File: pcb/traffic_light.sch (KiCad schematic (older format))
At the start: 48 parts, among them J1 Serial, J2 Power, Q1 BS170, Q2 BS170, Q3 BS170, SW1 RESET, SW2 FLASH, U1 ESP-12F, U2 LM1117-3.3

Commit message: start assigning footprints
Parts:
- U1: footprint (none) -> ESP8266:ESP-12E_SMD
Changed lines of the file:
@@
 F 0 "U1" H 6330 3085 50  0000 C CNN
 F 1 "ESP-12F" H 6330 2994 50  0000 C CNN
-F 2 "" H 6330 2320 50  0001 C CNN
+F 2 "ESP8266:ESP-12E_SMD" H 6330 2320 50  0001 C CNN
 F 3 "" H 6330 2320 50  0001 C CNN
 	1    6330 2320

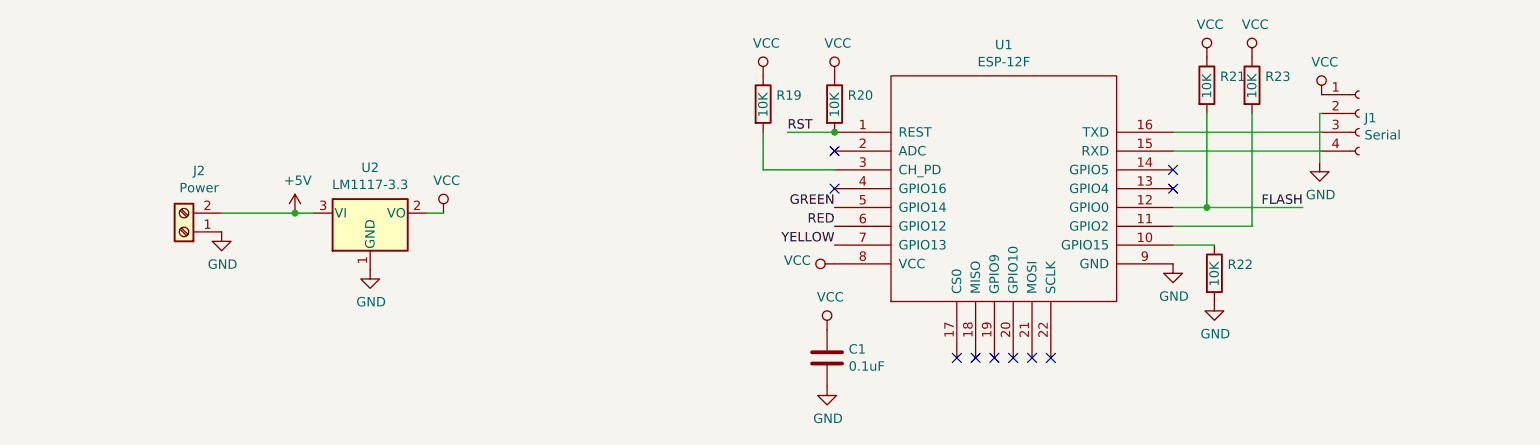
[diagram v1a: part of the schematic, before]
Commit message: start laying out the PCB
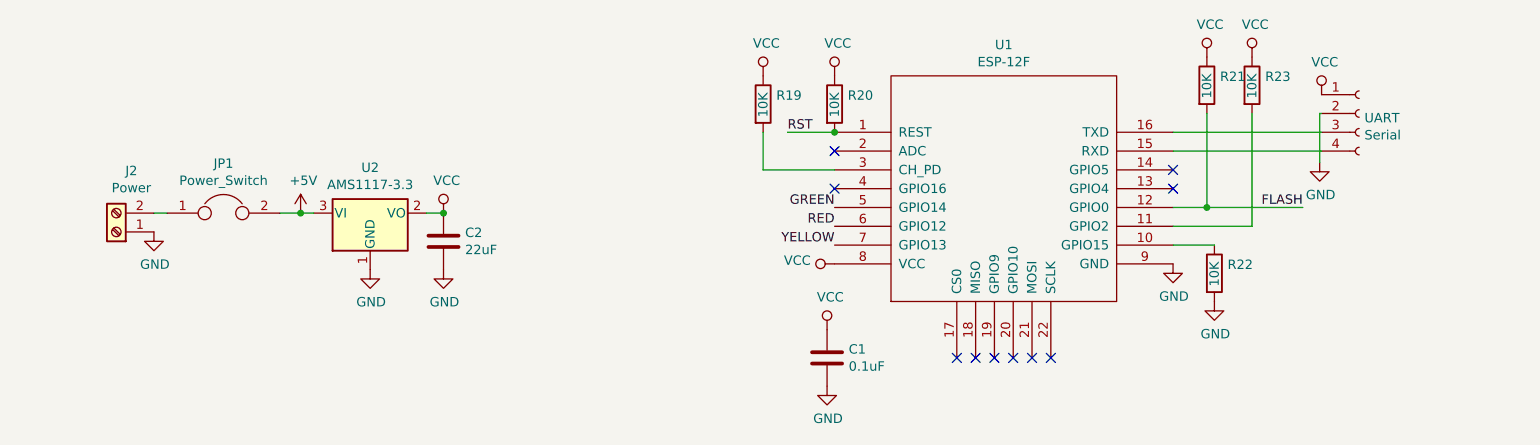
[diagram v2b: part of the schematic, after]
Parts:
- removed U2: LM1117-3.3, symbol Regulator_Linear:LM1117-3.3
- added C2: 22uF, Capacitor_SMD:C_1206_3216Metric, symbol Device:C
- added JP1: Power_Switch, Connector_PinHeader_2.54mm:PinHeader_1x02_P2.54mm_Vertical, symbol Device:Jumper
- added U2: AMS1117-3.3, Package_TO_SOT_SMD:SOT-223-3_TabPin2, symbol Regulator_Linear:AMS1117-3.3
- C1: footprint (none) -> Capacitor_SMD:C_1206_3216Metric
- D1, D10, D11, D12, D13, D14, D15, D2, D3, D4, D5, D6, D7, D8, D9: footprint (none) -> LED_THT:LED_D5.0mm
- J2: footprint (none) -> Connector_PinHeader_2.54mm:PinHeader_1x02_P2.54mm_Vertical
- R1, R10, R11, R12, R13, R14, R15, R16, R17, R18, R19, R2, R20, R21, R22, R23, R3, R4, R5, R6, R7, R8, R9: footprint Resistor_THT:R_Axial_DIN0207_L6.3mm_D2.5mm_P10.16mm_Horizontal -> Resistor_SMD:R_1206_3216Metric_Pad1.42x1.75mm_HandSolder
- SW1, SW2: footprint (none) -> Button_Switch_THT:SW_PUSH_6mm
- UART: renamed from J1; footprint Connector_PinHeader_2.54mm:PinHeader_1x04_P2.54mm_Horizontal -> Connector_PinHeader_2.54mm:PinHeader_1x04_P2.54mm_Vertical
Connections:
- net +5V: now also JP1.2, U2.3 (VI); no longer J2.2 (Pin_2)
- net GND: now also C2.2, U2.1 (GND)
- net VCC: now also C2.1, U2.2 (VO)
- new net: J2.2 (Pin_2), JP1.1
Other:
- moved on the sheet: J2

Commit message: laying out PCB
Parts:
- renumbered UART to UART1
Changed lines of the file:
@@
 NoConn ~ 5430 2320
 $Comp
-L Connector:Conn_01x04_Female UART
+L Connector:Conn_01x04_Female UART1
 U 1 1 5C0B813A
 P 8220 1920
-F 0 "UART" H 8248 1896 50  0000 L CNN
+F 0 "UART1" H 8248 1896 50  0000 L CNN
 F 1 "Serial" H 8248 1805 50  0000 L CNN
 F 2 "Connector_PinHeader_2.54mm:PinHeader_1x04_P2.54mm_Vertical" H 8220 1920 50  0001 C CNN

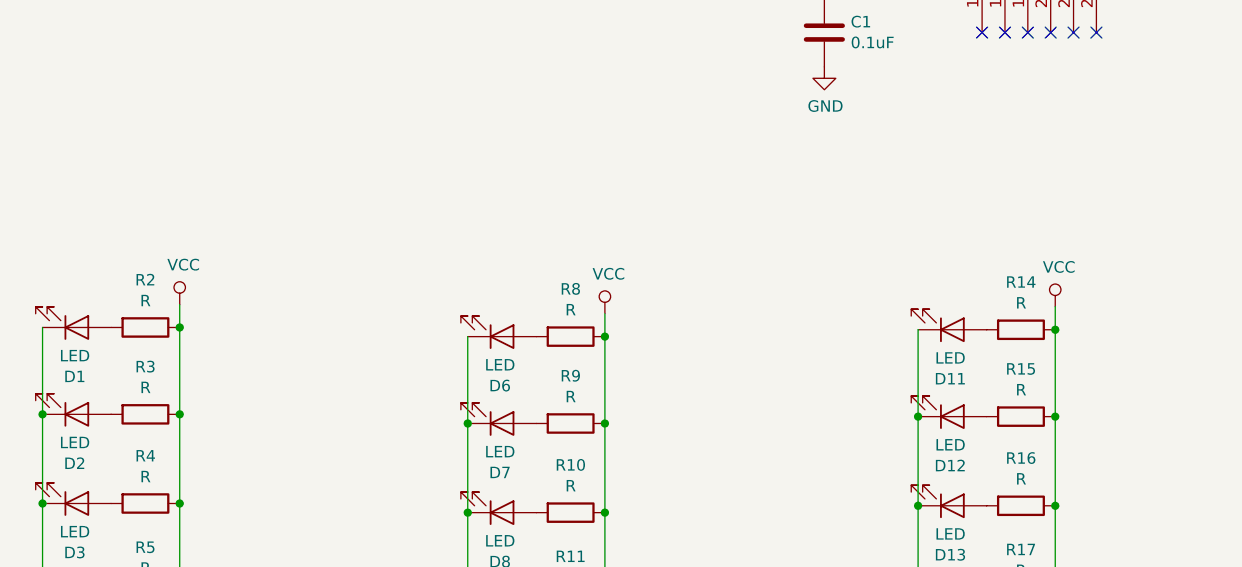
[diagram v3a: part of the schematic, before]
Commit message: place all components on the board
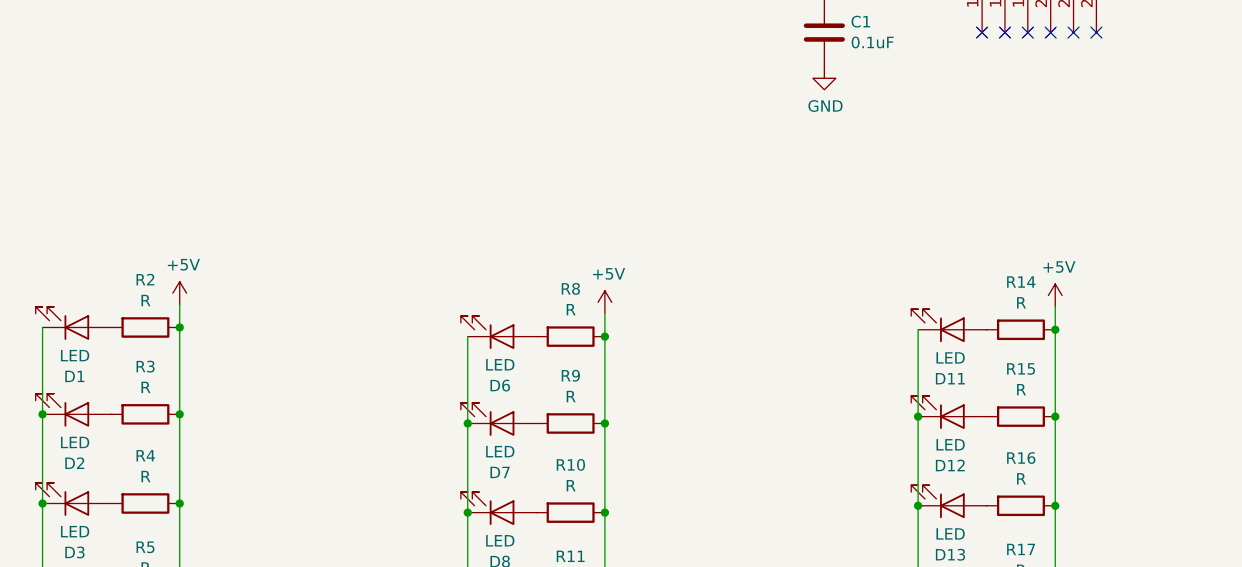
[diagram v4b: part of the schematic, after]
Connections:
- net +5V: now also R10.1, R11.1, R12.1, R14.1, R15.1, R16.1, R17.1, R18.1, R2.1, R3.1, R4.1, R5.1, R6.1, R8.1, R9.1
- net VCC: no longer R10.1, R11.1, R12.1, R14.1, R15.1, R16.1, R17.1, R18.1, R2.1, R3.1, R4.1, R5.1, R6.1, R8.1, R9.1
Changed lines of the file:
@@
 	2570 4890 2570 4510
 Connection ~ 2570 4890
-$Comp
-L power:VCC #PWR0103
-U 1 1 5C085669
-P 2570 4410
-F 0 "#PWR0103" H 2570 4260 50  0001 C CNN
-F 1 "VCC" H 2587 4583 50  0000 C CNN
-F 2 "" H 2570 4410 50  0001 C CNN
-F 3 "" H 2570 4410 50  0001 C CNN
-	1    2570 4410
-	1    0    0    -1
-$EndComp
 Wire Wire Line
 	2570 4410 2570 4510
@@
 	4430 4930 4430 4550
 Connection ~ 4430 4930
-$Comp
-L power:VCC #PWR0106
-U 1 1 5C087DA0
-P 4430 4450
-F 0 "#PWR0106" H 4430 4300 50  0001 C CNN
-F 1 "VCC" H 4447 4623 50  0000 C CNN
-F 2 "" H 4430 4450 50  0001 C CNN
-F 3 "" H 4430 4450 50  0001 C CNN
-	1    4430 4450
-	1    0    0    -1
-$EndComp
 Wire Wire Line
 	4430 4450 4430 4550
@@
 	6400 4900 6400 4520
 Connection ~ 6400 4900
-$Comp
-L power:VCC #PWR0109
-U 1 1 5C089E89
-P 6400 4420
-F 0 "#PWR0109" H 6400 4270 50  0001 C CNN
-F 1 "VCC" H 6417 4593 50  0000 C CNN
-F 2 "" H 6400 4420 50  0001 C CNN
-F 3 "" H 6400 4420 50  0001 C CNN
-	1    6400 4420
-	1    0    0    -1
-$EndComp
 Wire Wire Line
 	6400 4420 6400 4520
@@
 Wire Wire Line
 	1810 2450 1880 2450
+$Comp
+L power:+5V #PWR?
+U 1 1 5C0BA233
+P 4430 4450
+F 0 "#PWR?" H 4430 4300 50  0001 C CNN
+F 1 "+5V" H 4445 4623 50  0000 C CNN
+F 2 "" H 4430 4450 50  0001 C CNN
+F 3 "" H 4430 4450 50  0001 C CNN
+	1    4430 4450
+	1    0    0    -1
+$EndComp
+$Comp
+L power:+5V #PWR?
+U 1 1 5C0BC5A1
+P 2570 4410
+F 0 "#PWR?" H 2570 4260 50  0001 C CNN
+F 1 "+5V" H 2585 4583 50  0000 C CNN
+F 2 "" H 2570 4410 50  0001 C CNN
+F 3 "" H 2570 4410 50  0001 C CNN
+	1    2570 4410
+	1    0    0    -1
+$EndComp
+$Comp
+L power:+5V #PWR?
+U 1 1 5C0BC994
+P 6400 4420
+F 0 "#PWR?" H 6400 4270 50  0001 C CNN
+F 1 "+5V" H 6415 4593 50  0000 C CNN
+F 2 "" H 6400 4420 50  0001 C CNN
+F 3 "" H 6400 4420 50  0001 C CNN
+	1    6400 4420
+	1    0    0    -1
+$EndComp
 $EndSCHEMATC

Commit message: route everything
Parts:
- renumbered SW1 to BTN1, SW2 to BTN2, JP1 to SW1, J2 to VIN1
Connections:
- net at U1.15 (RXD): now also UART1.3 (Pin_3); no longer UART1.4 (Pin_4)
- net at U1.16 (TXD): now also UART1.4 (Pin_4); no longer UART1.3 (Pin_3)
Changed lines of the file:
@@
 Connection ~ 5430 2020
 $Comp
-L Switch:SW_Push SW2
+L Switch:SW_Push BTN2
 U 1 1 5C0ACC07
 P 9140 4580
-F 0 "SW2" V 9094 4728 50  0000 L CNN
-F 1 "FLASH" V 9185 4728 50  0000 L CNN
+F 0 "BTN2" V 9094 4728 50  0000 L CNN
+F 1 "FLASH" V 9185 4728 50  0001 L CNN
 F 2 "Button_Switch_THT:SW_PUSH_6mm" H 9140 4780 50  0001 C CNN
 F 3 "" H 9140 4780 50  0001 C CNN
@@
 $EndComp
 $Comp
-L Switch:SW_Push SW1
+L Switch:SW_Push BTN1
 U 1 1 5C0B00BA
 P 8480 4590
-F 0 "SW1" V 8434 4738 50  0000 L CNN
-F 1 "RESET" V 8525 4738 50  0000 L CNN
+F 0 "BTN1" V 8434 4738 50  0000 L CNN
+F 1 "RESET" V 8525 4738 50  0001 L CNN
 F 2 "Button_Switch_THT:SW_PUSH_6mm" H 8480 4790 50  0001 C CNN
 F 3 "" H 8480 4790 50  0001 C CNN
@@
 	1    0    0    -1
 $EndComp
-Wire Wire Line
-	7230 2120 8020 2120
-Wire Wire Line
-	7230 2020 8020 2020
 $Comp
 L power:VCC #PWR0121
@@
 L power:GND #PWR0122
 U 1 1 5C0BD64D
-P 8010 2180
-F 0 "#PWR0122" H 8010 1930 50  0001 C CNN
-F 1 "GND" H 8015 2007 50  0000 C CNN
-F 2 "" H 8010 2180 50  0001 C CNN
-F 3 "" H 8010 2180 50  0001 C CNN
-	1    8010 2180
-	1    0    0    -1
-$EndComp
-Wire Wire Line
-	8010 2180 8010 1920
-Wire Wire Line
-	8010 1920 8020 1920
+P 7950 2180
+F 0 "#PWR0122" H 7950 1930 50  0001 C CNN
+F 1 "GND" H 7955 2007 50  0000 C CNN
+F 2 "" H 7950 2180 50  0001 C CNN
+F 3 "" H 7950 2180 50  0001 C CNN
+	1    7950 2180
+	1    0    0    -1
+$EndComp
 NoConn ~ 6080 3220
 NoConn ~ 6180 3220
@@
 	3350 2450 3260 2450
 $Comp
-L Connector:Screw_Terminal_01x02 J2
+L Connector:Screw_Terminal_01x02 VIN1
 U 1 1 5C0DA213
 P 1610 2550
-F 0 "J2" H 1530 2225 50  0000 C CNN
-F 1 "Power" H 1530 2316 50  0000 C CNN
+F 0 "VIN1" H 1530 2225 50  0000 C CNN
+F 1 "Power" H 1530 2316 50  0001 C CNN
 F 2 "Connector_PinHeader_2.54mm:PinHeader_1x02_P2.54mm_Vertical" H 1610 2550 50  0001 C CNN
 F 3 "~" H 1610 2550 50  0001 C CNN
@@
 $EndComp
 $Comp
-L Device:Jumper JP1
+L Device:Jumper SW1
 U 1 1 5C0EB53D
 P 2180 2450
-F 0 "JP1" H 2180 2714 50  0000 C CNN
-F 1 "Power_Switch" H 2180 2623 50  0000 C CNN
+F 0 "SW1" H 2180 2714 50  0000 C CNN
+F 1 "Power_Switch" H 2180 2623 50  0001 C CNN
 F 2 "Connector_PinHeader_2.54mm:PinHeader_1x02_P2.54mm_Vertical" H 2180 2450 50  0001 C CNN
 F 3 "~" H 2180 2450 50  0001 C CNN
@@
 	1810 2450 1880 2450
 $Comp
-L power:+5V #PWR?
+L power:+5V #PWR0103
 U 1 1 5C0BA233
 P 4430 4450
-F 0 "#PWR?" H 4430 4300 50  0001 C CNN
+F 0 "#PWR0103" H 4430 4300 50  0001 C CNN
 F 1 "+5V" H 4445 4623 50  0000 C CNN
 F 2 "" H 4430 4450 50  0001 C CNN
@@
 $EndComp
 $Comp
-L power:+5V #PWR?
+L power:+5V #PWR0106
 U 1 1 5C0BC5A1
 P 2570 4410
-F 0 "#PWR?" H 2570 4260 50  0001 C CNN
+F 0 "#PWR0106" H 2570 4260 50  0001 C CNN
 F 1 "+5V" H 2585 4583 50  0000 C CNN
 F 2 "" H 2570 4410 50  0001 C CNN
@@
 $EndComp
 $Comp
-L power:+5V #PWR?
+L power:+5V #PWR0109
 U 1 1 5C0BC994
 P 6400 4420
-F 0 "#PWR?" H 6400 4270 50  0001 C CNN
+F 0 "#PWR0109" H 6400 4270 50  0001 C CNN
 F 1 "+5V" H 6415 4593 50  0000 C CNN
 F 2 "" H 6400 4420 50  0001 C CNN
@@
 	1    0    0    -1
 $EndComp
+Wire Wire Line
+	7230 2120 8020 2020
+Wire Wire Line
+	8020 2120 7230 2020
+Wire Wire Line
+	8020 1920 7950 1920
+Wire Wire Line
+	7950 1920 7950 2180
 $EndSCHEMATC

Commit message: final touches
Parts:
- added C3: 10uF, Capacitor_SMD:C_1206_3216Metric, symbol Device:C
- C2: value 22uF -> 10uF
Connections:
- net +5V: now also C3.1
- net GND: now also C3.2
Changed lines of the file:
@@
 P 3350 2600
 F 0 "C2" H 3465 2646 50  0000 L CNN
-F 1 "22uF" H 3465 2555 50  0000 L CNN
+F 1 "10uF" H 3465 2555 50  0000 L CNN
 F 2 "Capacitor_SMD:C_1206_3216Metric" H 3388 2450 50  0001 C CNN
 F 3 "~" H 3350 2600 50  0001 C CNN
@@
 Wire Wire Line
 	7950 1920 7950 2180
+$Comp
+L Device:C C3
+U 1 1 5C0BFCD0
+P 2590 2600
+F 0 "C3" H 2705 2646 50  0000 L CNN
+F 1 "10uF" H 2705 2555 50  0000 L CNN
+F 2 "Capacitor_SMD:C_1206_3216Metric" H 2628 2450 50  0001 C CNN
+F 3 "~" H 2590 2600 50  0001 C CNN
+	1    2590 2600
+	1    0    0    -1
+$EndComp
+$Comp
+L power:GND #PWR0128
+U 1 1 5C0C0456
+P 2590 2750
+F 0 "#PWR0128" H 2590 2500 50  0001 C CNN
+F 1 "GND" H 2595 2577 50  0000 C CNN
+F 2 "" H 2590 2750 50  0001 C CNN
+F 3 "" H 2590 2750 50  0001 C CNN
+	1    2590 2750
+	1    0    0    -1
+$EndComp
 $EndSCHEMATC

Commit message: Minor PCB improvements
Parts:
- removed SW1: Power_Switch, Connector_PinHeader_2.54mm:PinHeader_1x02_P2.54mm_Vertical, symbol Device:Jumper
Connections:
- net +5V: now also UART1.1 (Pin_1), VIN1.2 (Pin_2)
- net VCC: no longer UART1.1 (Pin_1)
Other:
- moved on the sheet: VIN1
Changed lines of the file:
@@
 EESchema Schematic File Version 4
 LIBS:traffic_light-cache
-EELAYER 26 0
+EELAYER 29 0
 EELAYER END
 $Descr A4 11693 8268
@@
 $EndComp
 $Comp
-L power:VCC #PWR0121
-U 1 1 5C0BD195
-P 8020 1820
-F 0 "#PWR0121" H 8020 1670 50  0001 C CNN
-F 1 "VCC" H 8037 1993 50  0000 C CNN
-F 2 "" H 8020 1820 50  0001 C CNN
-F 3 "" H 8020 1820 50  0001 C CNN
-	1    8020 1820
-	1    0    0    -1
-$EndComp
-$Comp
 L power:GND #PWR0122
 U 1 1 5C0BD64D
@@
 L Connector:Screw_Terminal_01x02 VIN1
 U 1 1 5C0DA213
-P 1610 2550
-F 0 "VIN1" H 1530 2225 50  0000 C CNN
-F 1 "Power" H 1530 2316 50  0001 C CNN
-F 2 "Connector_PinHeader_2.54mm:PinHeader_1x02_P2.54mm_Vertical" H 1610 2550 50  0001 C CNN
-F 3 "~" H 1610 2550 50  0001 C CNN
-	1    1610 2550
+P 2210 2550
+F 0 "VIN1" H 2130 2225 50  0000 C CNN
+F 1 "Power" H 2130 2316 50  0001 C CNN
+F 2 "Connector_PinHeader_2.54mm:PinHeader_1x02_P2.54mm_Vertical" H 2210 2550 50  0001 C CNN
+F 3 "~" H 2210 2550 50  0001 C CNN
+	1    2210 2550
 	-1   0    0    1
 $EndComp
@@
 L power:GND #PWR0126
 U 1 1 5C0DD276
-P 1810 2550
-F 0 "#PWR0126" H 1810 2300 50  0001 C CNN
-F 1 "GND" H 1815 2377 50  0000 C CNN
-F 2 "" H 1810 2550 50  0001 C CNN
-F 3 "" H 1810 2550 50  0001 C CNN
-	1    1810 2550
+P 2410 2550
+F 0 "#PWR0126" H 2410 2300 50  0001 C CNN
+F 1 "GND" H 2415 2377 50  0000 C CNN
+F 2 "" H 2410 2550 50  0001 C CNN
+F 3 "" H 2410 2550 50  0001 C CNN
+	1    2410 2550
 	1    0    0    -1
 $EndComp
@@
 	1    0    0    -1
 $EndComp
-$Comp
-L Device:Jumper SW1
-U 1 1 5C0EB53D
-P 2180 2450
-F 0 "SW1" H 2180 2714 50  0000 C CNN
-F 1 "Power_Switch" H 2180 2623 50  0001 C CNN
-F 2 "Connector_PinHeader_2.54mm:PinHeader_1x02_P2.54mm_Vertical" H 2180 2450 50  0001 C CNN
-F 3 "~" H 2180 2450 50  0001 C CNN
-	1    2180 2450
-	1    0    0    -1
-$EndComp
 Wire Wire Line
 	2660 2450 2590 2450
-Wire Wire Line
-	2480 2450 2590 2450
 Connection ~ 2590 2450
-Wire Wire Line
-	1810 2450 1880 2450
 $Comp
 L power:+5V #PWR0103
@@
 	1    0    0    -1
 $EndComp
+$Comp
+L power:+5V #PWR0121
+U 1 1 5CC9FB36
+P 8020 1820
+F 0 "#PWR0121" H 8020 1670 50  0001 C CNN
+F 1 "+5V" H 8035 1993 50  0000 C CNN
+F 2 "" H 8020 1820 50  0001 C CNN
+F 3 "" H 8020 1820 50  0001 C CNN
+	1    8020 1820
+	1    0    0    -1
+$EndComp
+Wire Wire Line
+	2410 2450 2590 2450
 $EndSCHEMATC
